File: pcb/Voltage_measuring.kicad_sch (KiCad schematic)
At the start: 4 parts, among them Q4 UT6MA2TCR

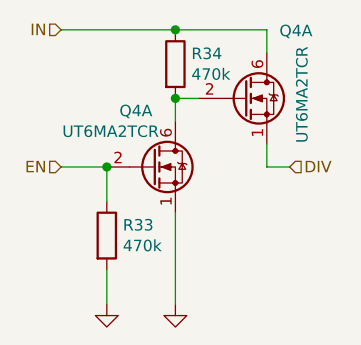
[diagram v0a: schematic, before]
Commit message: Schema: update connection of CS_EN pin
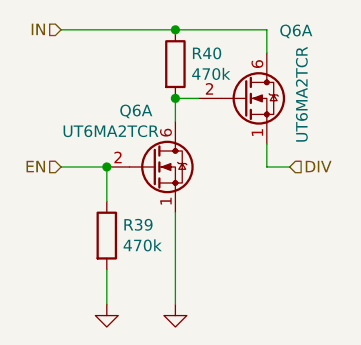
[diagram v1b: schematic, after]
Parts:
- renumbered Q4 to Q6, R33 to R39, R34 to R40
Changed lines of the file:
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@@
   (symbol (lib_id "power:GND") (at 93.98 115.57 0)
     (in_bom yes) (on_board yes)
-    (property "Reference" "#PWR078" (id 0) (at 93.98 121.92 0)
+    (property "Reference" "#PWR091" (id 0) (at 93.98 121.92 0)
       (effects (font (size 1.27 1.27)) hide)
     )
@@
   (symbol (lib_id "power:GND") (at 101.6 115.57 0)
     (in_bom yes) (on_board yes)
-    (property "Reference" "#PWR079" (id 0) (at 101.6 121.92 0)
+    (property "Reference" "#PWR092" (id 0) (at 101.6 121.92 0)
       (effects (font (size 1.27 1.27)) hide)
     )
@@
   (symbol (lib_id "Device:R") (at 93.98 107.95 0)
     (in_bom yes) (on_board yes)
-    (property "Reference" "R33" (id 0) (at 95.7581 106.8006 0)
+    (property "Reference" "R39" (id 0) (at 95.7581 106.8006 0)
       (effects (font (size 1.27 1.27)) (justify left))
     )
@@
   (symbol (lib_id "Device:R") (at 101.6 88.9 0)
     (in_bom yes) (on_board yes)
-    (property "Reference" "R34" (id 0) (at 103.3781 87.7506 0)
+    (property "Reference" "R40" (id 0) (at 103.3781 87.7506 0)
       (effects (font (size 1.27 1.27)) (justify left))
     )
@@
   (symbol (lib_id "TCY_IC:UT6MA2TCR") (at 99.06 100.33 0)
     (in_bom yes) (on_board yes)
-    (property "Reference" "Q4" (id 0) (at 95.3771 94.1006 0)
+    (property "Reference" "Q6" (id 0) (at 95.3771 94.1006 0)
       (effects (font (size 1.27 1.27)) (justify left))
     )
@@
   (symbol (lib_id "TCY_IC:UT6MA2TCR") (at 109.22 92.71 0)
     (in_bom yes) (on_board yes)
-    (property "Reference" "Q4" (id 0) (at 113.1571 85.2106 0)
+    (property "Reference" "Q6" (id 0) (at 113.1571 85.2106 0)
       (effects (font (size 1.27 1.27)) (justify left))
     )

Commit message: Schema: bom optimization
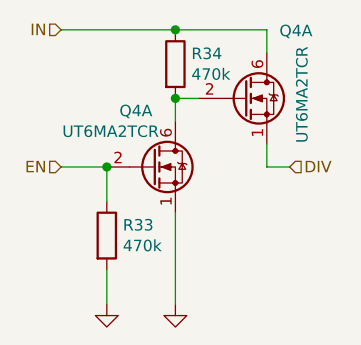
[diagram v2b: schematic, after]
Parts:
- renumbered Q6 to Q4, R39 to R33, R40 to R34
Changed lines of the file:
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@@
   (symbol (lib_id "Device:R") (at 93.98 107.95 0)
     (in_bom yes) (on_board yes)
-    (property "Reference" "R39" (id 0) (at 95.7581 106.8006 0)
+    (property "Reference" "R33" (id 0) (at 95.7581 106.8006 0)
       (effects (font (size 1.27 1.27)) (justify left))
     )
@@
   (symbol (lib_id "Device:R") (at 101.6 88.9 0)
     (in_bom yes) (on_board yes)
-    (property "Reference" "R40" (id 0) (at 103.3781 87.7506 0)
+    (property "Reference" "R34" (id 0) (at 103.3781 87.7506 0)
       (effects (font (size 1.27 1.27)) (justify left))
     )
@@
   (symbol (lib_id "TCY_IC:UT6MA2TCR") (at 99.06 100.33 0)
     (in_bom yes) (on_board yes)
-    (property "Reference" "Q6" (id 0) (at 95.3771 94.1006 0)
+    (property "Reference" "Q4" (id 0) (at 95.3771 94.1006 0)
       (effects (font (size 1.27 1.27)) (justify left))
     )
@@
   (symbol (lib_id "TCY_IC:UT6MA2TCR") (at 109.22 92.71 0)
     (in_bom yes) (on_board yes)
-    (property "Reference" "Q6" (id 0) (at 113.1571 85.2106 0)
+    (property "Reference" "Q4" (id 0) (at 113.1571 85.2106 0)
       (effects (font (size 1.27 1.27)) (justify left))
     )
